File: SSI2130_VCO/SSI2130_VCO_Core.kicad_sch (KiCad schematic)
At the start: 1 part, among them U3 SSI2130

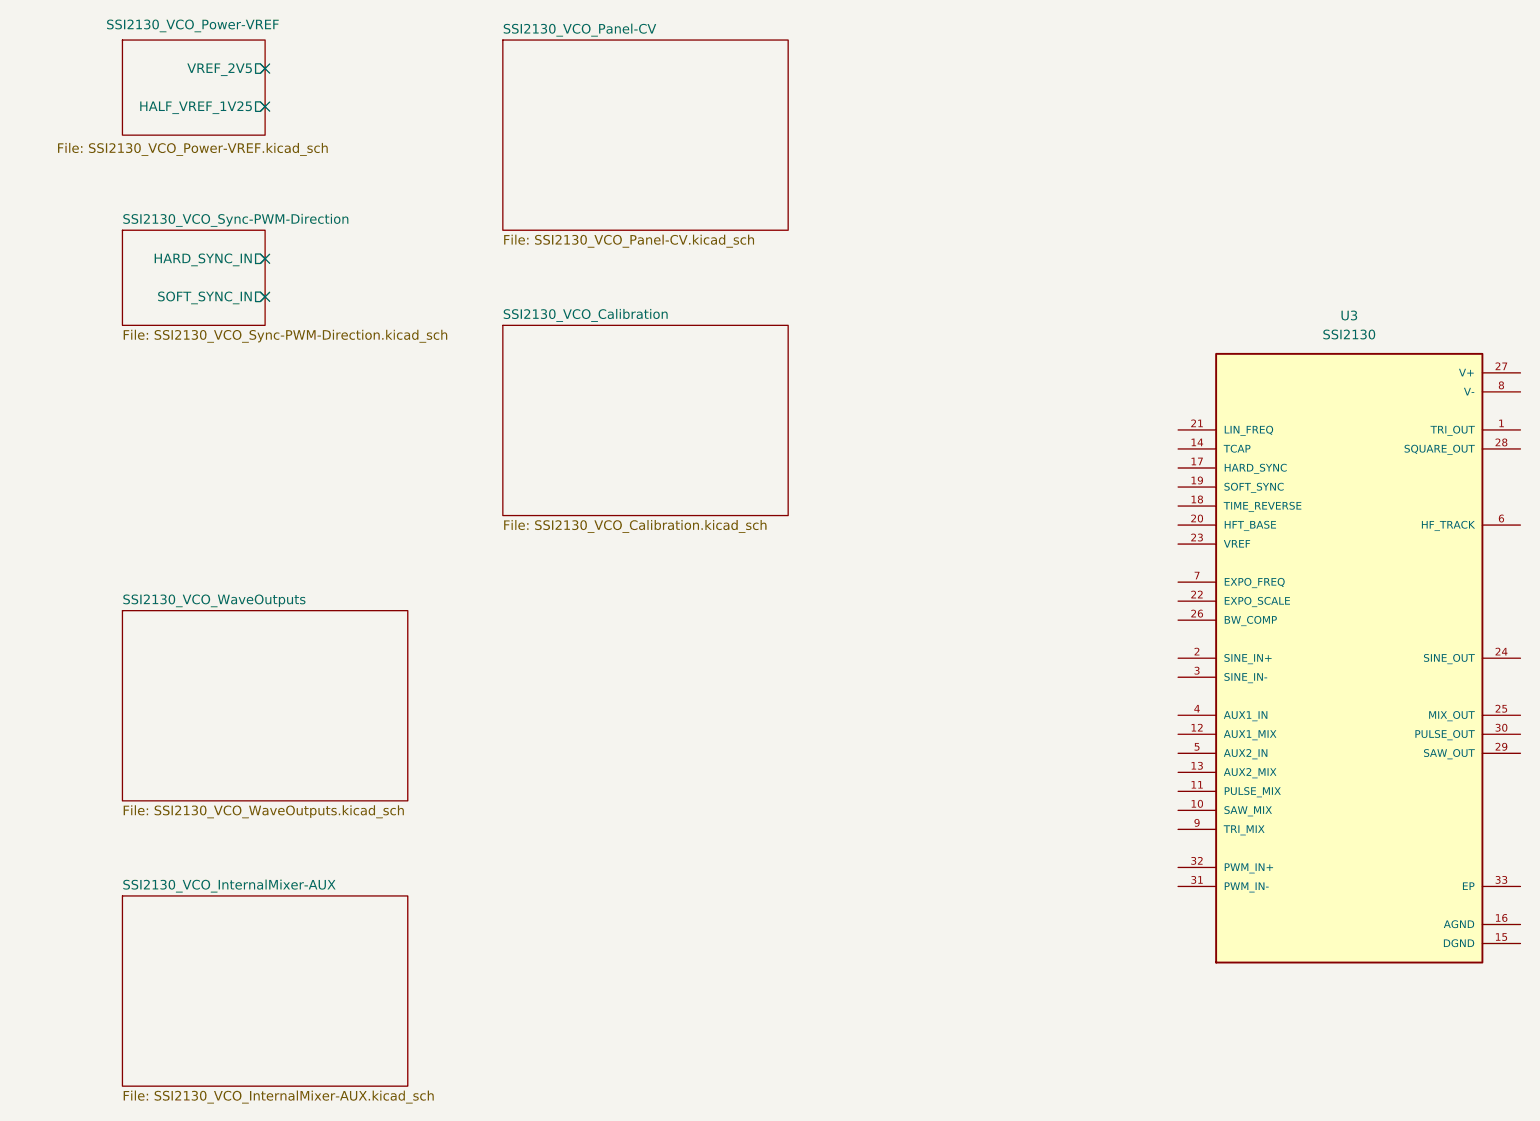
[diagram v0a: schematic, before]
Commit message: add TZ circuit
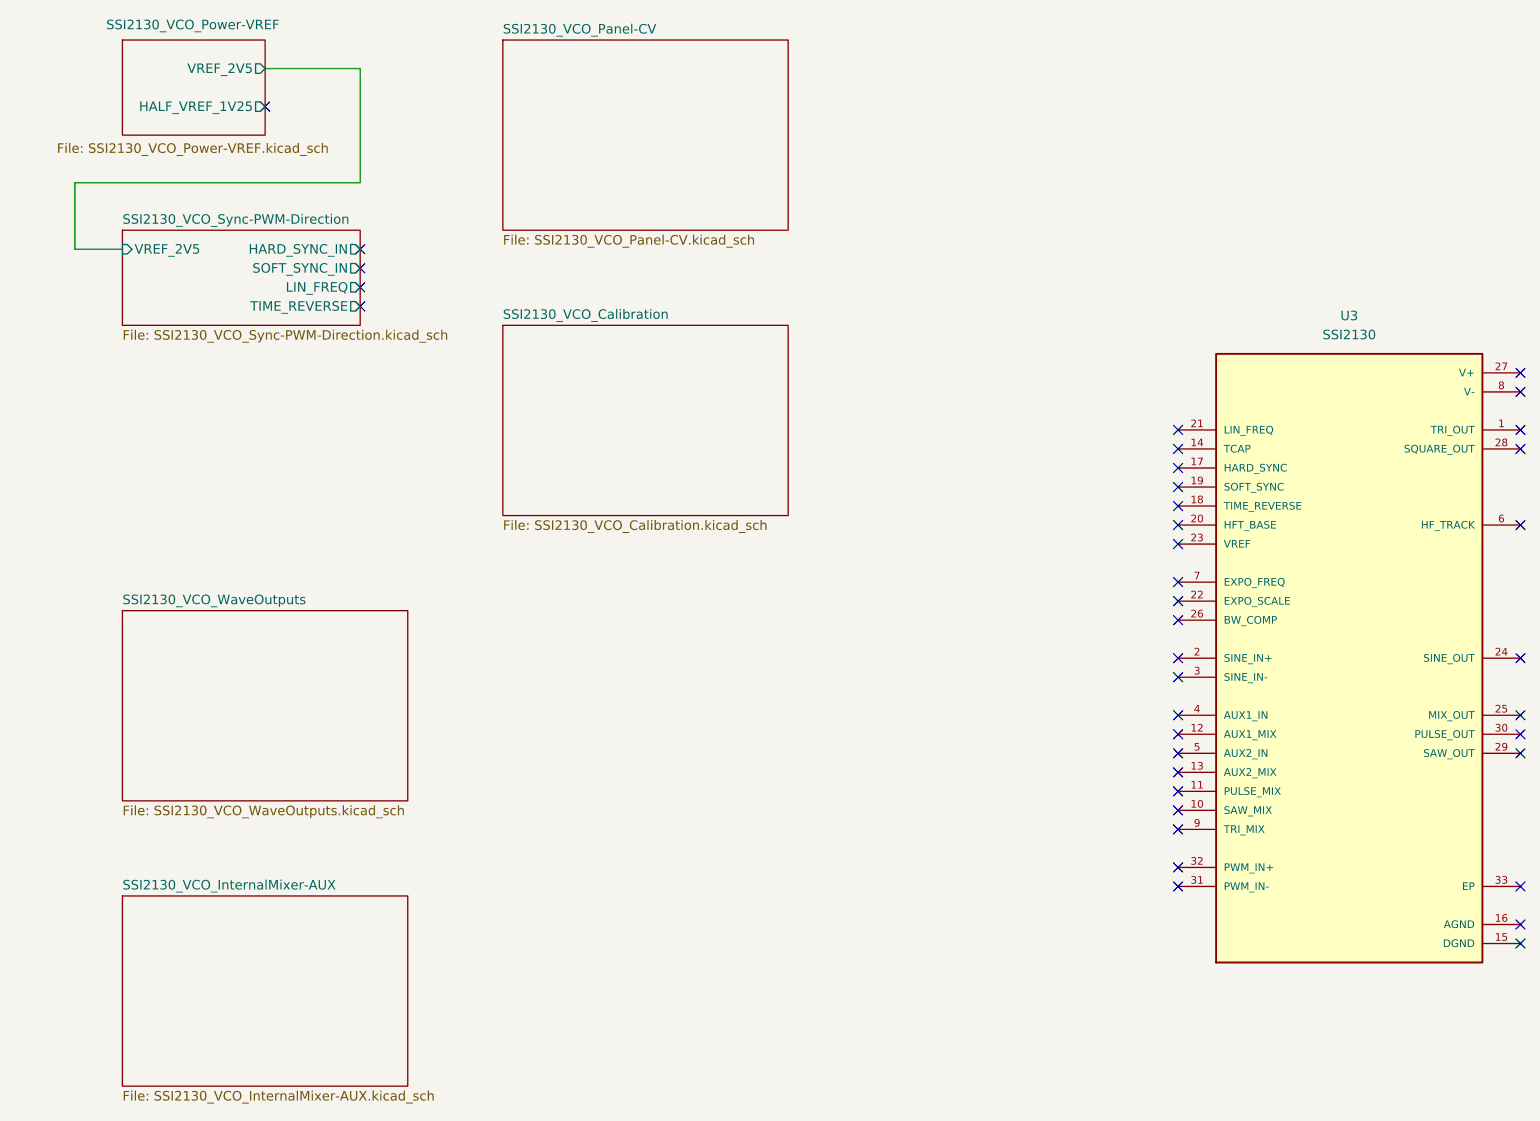
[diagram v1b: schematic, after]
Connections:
- no-connect marks 4 -> 38
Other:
- sheet SSI2130_VCO_Sync-PWM-Direction ports: added LIN_FREQ, TIME_REVERSE, VREF_2V5; removed none
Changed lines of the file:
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@@
 	(paper "A4")
 	(no_connect
-		(at 44.45 29.21)
+		(at 212.09 72.39)
+	)
+	(no_connect
+		(at 166.37 80.01)
+	)
+	(no_connect
+		(at 166.37 100.33)
+	)
+	(no_connect
+		(at 166.37 110.49)
+	)
+	(no_connect
+		(at 166.37 120.65)
+	)
+	(no_connect
+		(at 166.37 82.55)
+	)
+	(no_connect
+		(at 166.37 118.11)
+	)
+	(no_connect
+		(at 212.09 80.01)
+	)
+	(no_connect
+		(at 166.37 123.19)
+	)
+	(no_connect
+		(at 166.37 90.17)
+	)
+	(no_connect
+		(at 166.37 92.71)
+	)
+	(no_connect
+		(at 166.37 102.87)
+	)
+	(no_connect
+		(at 57.15 55.88)
+	)
+	(no_connect
+		(at 212.09 69.85)
+	)
+	(no_connect
+		(at 166.37 85.09)
+	)
+	(no_connect
+		(at 212.09 115.57)
+	)
+	(no_connect
+		(at 212.09 90.17)
 	)
 	(no_connect
@@
 	)
 	(no_connect
-		(at 44.45 54.61)
-	)
-	(no_connect
-		(at 44.45 59.69)
+		(at 166.37 135.89)
+	)
+	(no_connect
+		(at 166.37 115.57)
+	)
+	(no_connect
+		(at 166.37 87.63)
+	)
+	(no_connect
+		(at 212.09 120.65)
+	)
+	(no_connect
+		(at 166.37 138.43)
+	)
+	(no_connect
+		(at 212.09 118.11)
+	)
+	(no_connect
+		(at 166.37 77.47)
+	)
+	(no_connect
+		(at 212.09 107.95)
+	)
+	(no_connect
+		(at 166.37 125.73)
+	)
+	(no_connect
+		(at 212.09 143.51)
+	)
+	(no_connect
+		(at 212.09 77.47)
+	)
+	(no_connect
+		(at 166.37 128.27)
+	)
+	(no_connect
+		(at 57.15 60.96)
+	)
+	(no_connect
+		(at 166.37 107.95)
+	)
+	(no_connect
+		(at 166.37 97.79)
+	)
+	(no_connect
+		(at 166.37 130.81)
+	)
+	(no_connect
+		(at 57.15 53.34)
+	)
+	(no_connect
+		(at 212.09 146.05)
+	)
+	(no_connect
+		(at 212.09 138.43)
+	)
+	(no_connect
+		(at 57.15 58.42)
+	)
+	(wire
+		(pts
+			(xy 44.45 29.21) (xy 57.15 29.21)
+		)
+		(stroke
+			(width 0)
+			(type default)
+		)
+	)
+	(wire
+		(pts
+			(xy 19.05 44.45) (xy 19.05 53.34)
+		)
+		(stroke
+			(width 0)
+			(type default)
+		)
+	)
+	(wire
+		(pts
+			(xy 57.15 29.21) (xy 57.15 44.45)
+		)
+		(stroke
+			(width 0)
+			(type default)
+		)
+	)
+	(wire
+		(pts
+			(xy 19.05 53.34) (xy 25.4 53.34)
+		)
+		(stroke
+			(width 0)
+			(type default)
+		)
+	)
+	(wire
+		(pts
+			(xy 57.15 44.45) (xy 19.05 44.45)
+		)
+		(stroke
+			(width 0)
+			(type default)
+		)
 	)
 	(symbol
@@
 	(sheet
 		(at 25.4 50.8)
-		(size 19.05 12.7)
+		(size 31.75 12.7)
 		(exclude_from_sim no)
 		(in_bom yes)
@@
 		)
 		(pin "SOFT_SYNC_IN" output
-			(at 44.45 59.69 0)
+			(at 57.15 55.88 0)
 			(effects
 				(font
@@
 		)
 		(pin "HARD_SYNC_IN" output
-			(at 44.45 54.61 0)
+			(at 57.15 53.34 0)
 			(effects
 				(font
@@
 			)
 		)
+		(pin "LIN_FREQ" output
+			(at 57.15 58.42 0)
+			(effects
+				(font
+					(size 1.27 1.27)
+				)
+				(justify right)
+			)
+		)
+		(pin "TIME_REVERSE" output
+			(at 57.15 60.96 0)
+			(effects
+				(font
+					(size 1.27 1.27)
+				)
+				(justify right)
+			)
+		)
+		(pin "VREF_2V5" input
+			(at 25.4 53.34 180)
+			(effects
+				(font
+					(size 1.27 1.27)
+				)
+				(justify left)
+			)
+		)
